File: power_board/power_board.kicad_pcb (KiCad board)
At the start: 2 copper layers, 165.3 x 121.3 mm, 66 parts, among them J1 PROG, J10 M4, J11 5V_1, J12 M5, J13 M6, J14 M7, J15 FAN, J16 Screw_Terminal_01x02, J17 MB_interface, J19 12V_1, J2 M1, J20 12V_2, J21 12V_3, J22 12V_4, J23 48V_1, J24 48V_2, J25 48V_3, J26 48V_4, J3 M2, J4 Conn_01x02_Female, J5 Conn_01x02_Female, J6 Conn_01x01_Male, J7 Conn_01x01_Male, J8 Screw_Terminal_01x02, J9 M3, Q1 2N3906, SW1 SW_Push, U1 ACS758xCB-050B-PFF, U2 ACS758xCB-050B-PFF, U3 MCP2515-EST, U4 MAX31855KASA, U5 MCP2551-I-SN, U6 BTS50085-1TMA, U7 ATmega328P-AU, U8 BTS50085-1TMA, U9 LM2596S-5, Y1 20Mhz, Y2 16Mhz

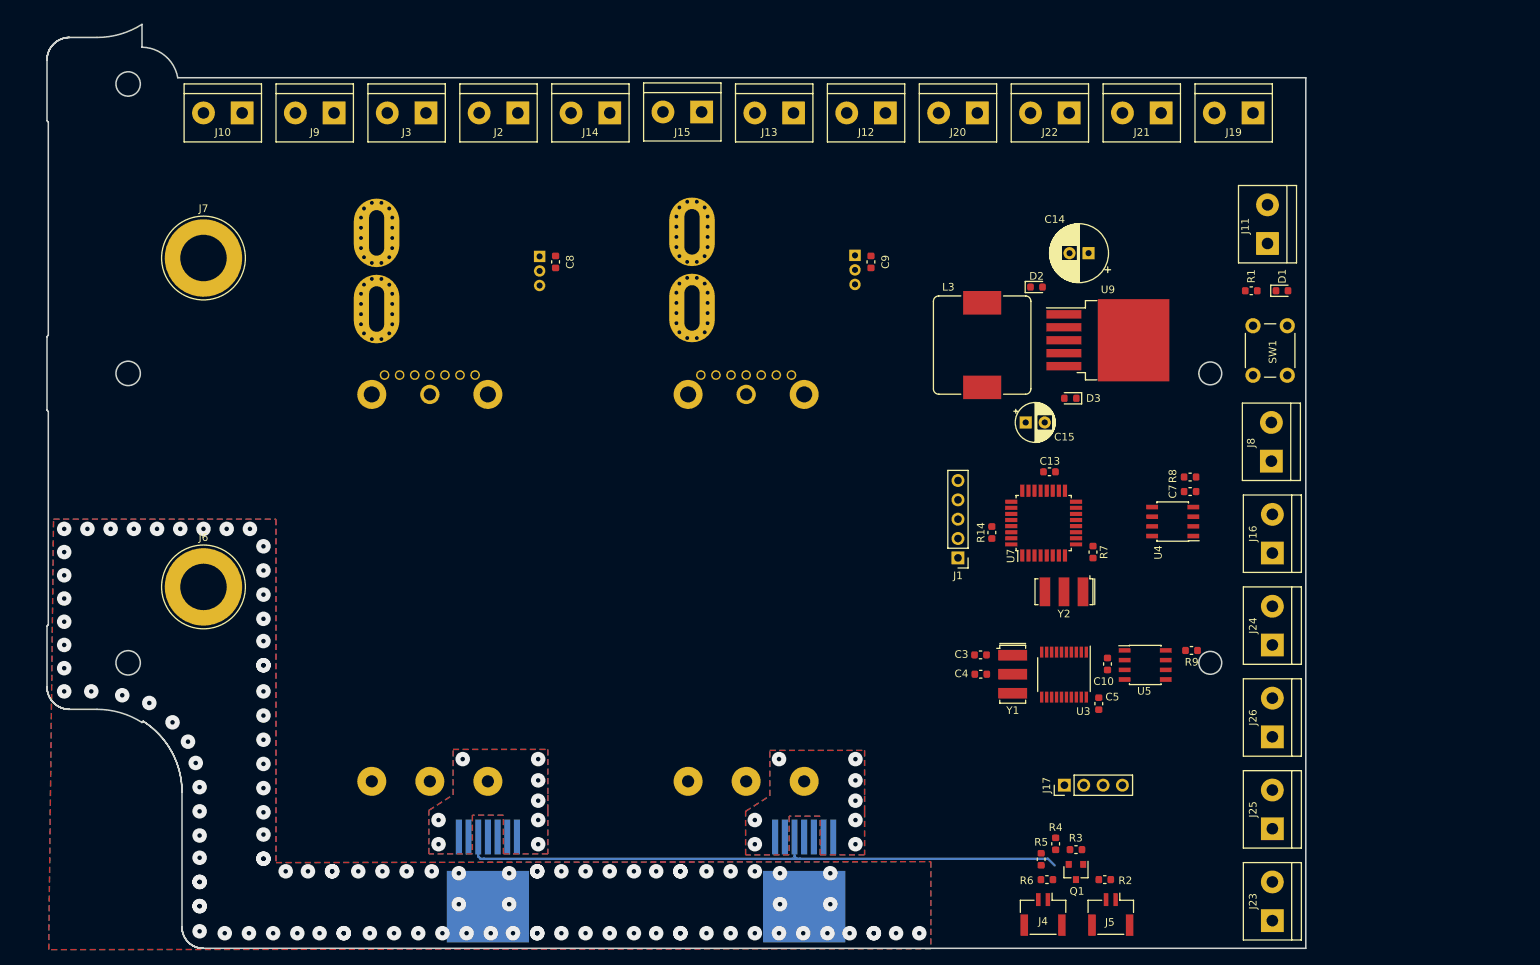
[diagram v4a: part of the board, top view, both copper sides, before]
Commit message: Finished high power routing
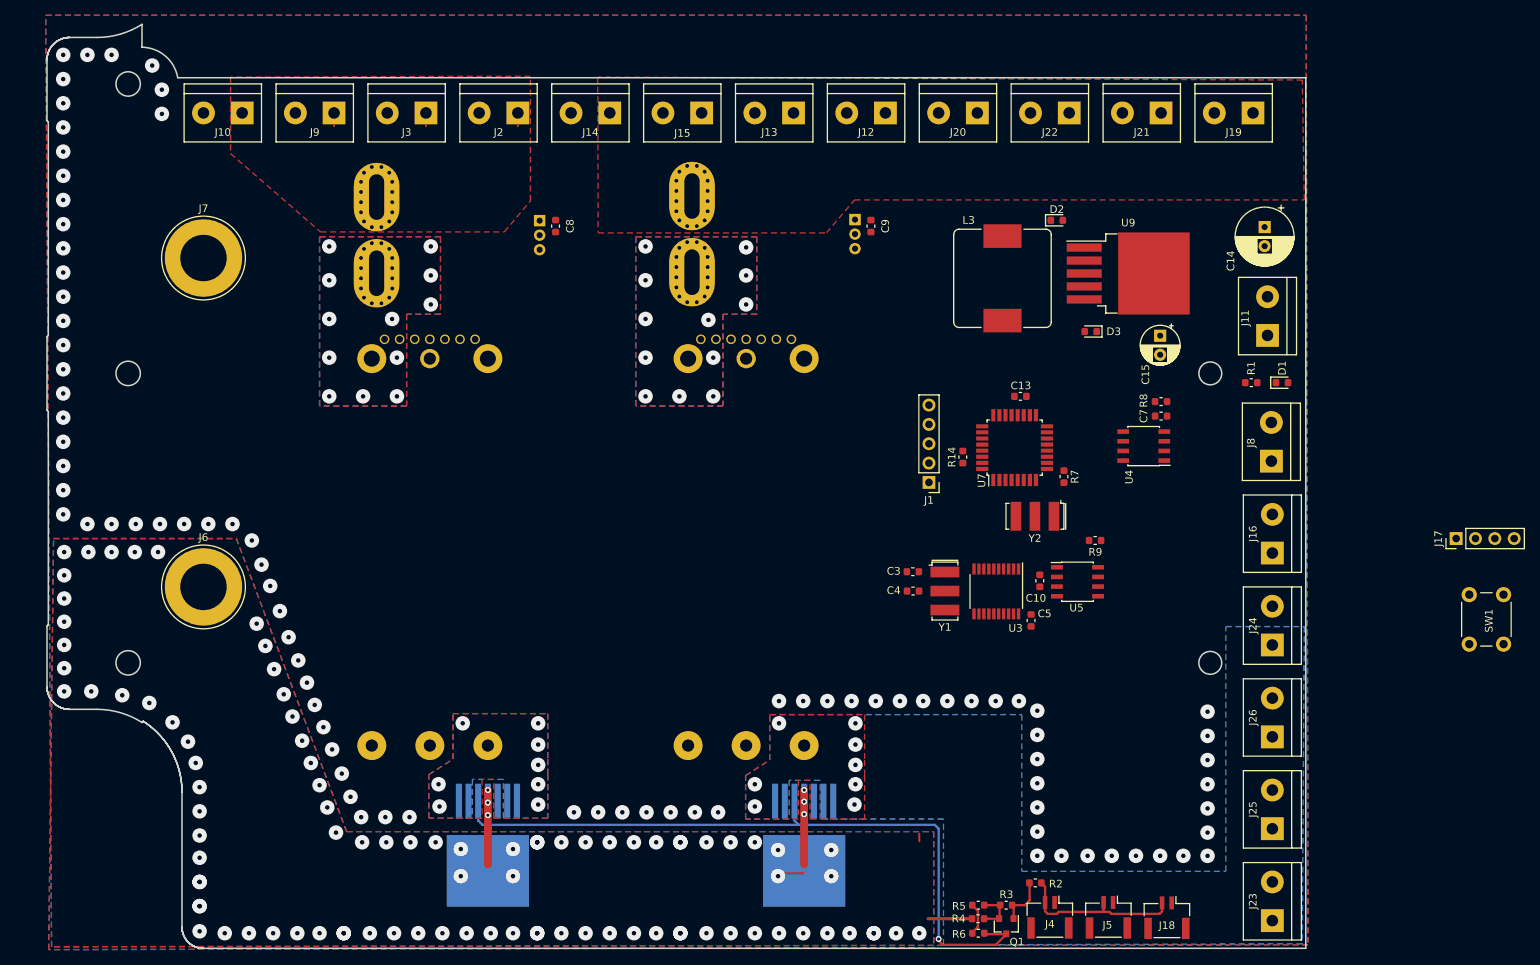
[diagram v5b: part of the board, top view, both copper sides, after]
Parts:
- added J18: Conn_01x02_Female, Connector_JST:JST_GH_BM02B-GHS-TBT_1x02-1MP_P1.25mm_Vertical, F.Cu at (207.8, 147.6)
- moved J17 60.8 mm to (245.7, 97.8)
- moved SW1 45.3 mm to (252.0, 105.2)
- moved C14 23.4 mm to (220.6, 56.9), turned to 270 degrees
- moved C15 21.0 mm to (206.9, 71.2), turned to 270 degrees
- moved R9 19.2 mm to (198.3, 98.0)
- moved R4 14.2 mm to (183.0, 147.7), turned to 180 degrees
- moved C10 14.1 mm to (191.1, 103.3)
- moved C5 14.1 mm to (189.9, 108.5)
- moved U3 14.1 mm to (185.4, 104.7)
- moved U5 14.1 mm to (196.0, 103.5)
- moved C3 14.1 mm to (174.4, 102.1)
- moved C4 14.1 mm to (174.4, 104.7)
- moved Y1 14.1 mm to (178.6, 104.7)
- moved J11 12.1 mm to (221.0, 71.1)
- moved D1 12.1 mm to (222.9, 77.3)
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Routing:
- net +48V: track 0.00 -> 29.6 mm, vias 109 -> 100
- net Net-(J18-Pad2): track 0.00 -> 22.2 mm
- net SHUTOFF: track 82.2 -> 94.4 mm, vias 0 -> 1
- net Net-(Q1-Pad1): track 0.00 -> 6.92 mm
- net +5VA: track 0.00 -> 6.10 mm
- net +12V: track 0.00 -> 5.25 mm
- net GNDREF: track 0.00 -> 4.34 mm, vias 0 -> 85
- net 12V_IN: vias 0 -> 12
- net 12VA_IN: vias 0 -> 12
- added copper zone on F.Cu, net +12V
- added copper zone on F.Cu, net +12VA
- added copper zone on B.Cu, net 12VA_IN
- added copper zone on F.Cu, net 12VA_IN
- added copper zone on B.Cu, net 12V_IN
- added copper zone on F.Cu, net 12V_IN
- added copper zone on B.Cu, net GNDREF
- added copper zone on F.Cu, net GNDREF

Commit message: Current sensor routing/finishing touches
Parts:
- moved J1 65.9 mm to (242.4, 89.5), turned to 270 degrees
- moved Y2 59.9 mm to (246.6, 74.2), turned to 270 degrees
- moved R14 58.0 mm to (238.9, 83.7), turned to 180 degrees
- moved R7 50.9 mm to (241.4, 70.4), turned to 0 degrees
- moved U7 50.6 mm to (237.6, 76.9), turned to 180 degrees
- moved C13 42.5 mm to (230.9, 76.1), turned to 270 degrees
- moved C5 21.2 mm to (211.1, 107.4)
- moved Y1 20.4 mm to (196.0, 94.0)
- moved U3 20.4 mm to (202.8, 94.1)
- moved C3 19.9 mm to (191.3, 91.6)
- moved C4 19.9 mm to (191.3, 94.1)
- moved C10 18.7 mm to (208.5, 96.7)
- moved U5 18.5 mm to (213.2, 96.6)
- moved R9 17.5 mm to (215.1, 93.0), turned to 0 degrees
- moved C7 8.52 mm to (215.4, 83.2)
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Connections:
- J16 pad 1: CANH -> CANL
- J16 pad 2: CANL -> CANH
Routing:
- net +5V: track 0.00 -> 88.6 mm, vias 0 -> 2
- net 12V_SENSE: track 0.00 -> 61.3 mm, vias 0 -> 2
- net 12VA_SENSE: track 0.00 -> 22.0 mm, vias 0 -> 1
- net GNDREF: vias 85 -> 97

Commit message: working on microcontroller routing
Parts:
- D2, D3: footprint Diode_SMD:D_0603_1608Metric -> Diode_SMD:D_SMB
- moved Y2 48.3 mm to (198.5, 78.2)
- moved C13 48.2 mm to (182.8, 79.0)
- moved U7 48.2 mm to (189.5, 79.8)
- moved R7 47.3 mm to (203.1, 98.0), turned to 270 degrees
- moved SW1 46.6 mm to (217.7, 73.7), turned to 0 degrees
- moved J17 41.4 mm to (204.9, 104.0)
- moved J1 40.9 mm to (206.4, 70.2), turned to 0 degrees
- moved C15 27.7 mm to (180.3, 63.2), turned to 90 degrees
- moved R14 26.5 mm to (215.7, 70.7)
- moved D3 15.4 mm to (182.4, 69.5), turned to 90 degrees
- moved D2 13.0 mm to (180.3, 56.3), turned to 180 degrees
- moved C5 11.3 mm to (204.9, 98.0)
- moved L3 5.53 mm to (191.4, 61.8)
- moved R1 4.83 mm to (223.9, 70.7), turned to 0 degrees
- moved D1 3.07 mm to (219.8, 70.7), turned to 180 degrees
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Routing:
- net +5V: track 88.6 -> 124.5 mm, vias 2 -> 3
- net Net-(C15-Pad1): track 0.00 -> 26.5 mm
- net Net-(D2-Pad1): track 0.00 -> 20.2 mm
- net GNDREF: track 4.34 -> 20.0 mm, vias 97 -> 101
- net Net-(J8-Pad2): track 0.00 -> 7.34 mm
- net CANH: track 0.00 -> 6.51 mm
- net CANL: track 0.00 -> 6.36 mm
- net Net-(J8-Pad1): track 0.00 -> 5.76 mm
- net TC_CS: track 0.00 -> 4.79 mm
- net CAN_CS: track 0.00 -> 2.37 mm
- net Net-(R9-Pad2): track 0.00 -> 1.75 mm

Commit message: finishing touches
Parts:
- Y2: footprint Crystal:Resonator_SMD-3Pin_7.2x3.0mm -> CSTCE16M0V53-R0:OSC_CSTCE16M0V53-R0
- moved C2 92.1 mm to (140.6, 139.6), turned to 90 degrees
- moved C1 30.7 mm to (69.2, 101.2), turned to 90 degrees
- moved R7 11.9 mm to (191.1, 97.8)
- moved Y1 11.9 mm to (183.0, 91.7)
- moved C3 11.9 mm to (178.2, 89.3)
- moved C4 11.9 mm to (178.3, 91.9)
- moved C5 11.9 mm to (192.9, 97.8)
- moved U3 11.9 mm to (189.7, 91.8)
- moved J17 8.14 mm to (196.7, 103.5)
- moved J1 3.39 mm to (203.1, 71.0)
- moved Y2 2.10 mm to (196.6, 77.3)
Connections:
- C1 pad 1: Net-(C1-Pad1) -> +48V
- C2 pad 1: 48V -> +48V
- J1 pad 3: TX -> RX
- J1 pad 4: RX -> TX
- J17 pad 1: +5V -> GNDREF
- J17 pad 4: GNDREF -> +5V
- REG1 pad 1: Net-(C1-Pad1) -> Net-(REG1-Pad1)
- U6 pad 1: Net-(C1-Pad1) -> Net-(REG1-Pad1)
- U6 pad 2: Net-(C1-Pad1) -> Net-(REG1-Pad1)
- U6 pad 6: Net-(C1-Pad1) -> Net-(REG1-Pad1)
- U6 pad 7: Net-(C1-Pad1) -> Net-(REG1-Pad1)
- U7 pad 1: RX_INT -> CAN_INT
- U7 pad 10: TC_CS -> Net-(U7-Pad10)
- U7 pad 2: Net-(U7-Pad2) -> TC_CS
- U7 pad 23: 12V_SENSE -> 12VA_SENSE
- U7 pad 24: 12VA_SENSE -> 12V_SENSE
- U7 pad 26: TX0RTS -> TX2RTS
- U7 pad 28: TX2RTS -> TX0RTS
- U7 pad 32: CAN_INT -> RX_INT
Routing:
- net GNDREF: track 20.0 -> 178.7 mm, vias 101 -> 119
- net +5V: track 124.5 -> 281.3 mm, vias 3 -> 5
- net RESET: track 0.00 -> 51.9 mm, vias 0 -> 3
- net SCK: track 0.00 -> 46.7 mm, vias 0 -> 4
- net MISO: track 0.00 -> 43.9 mm, vias 0 -> 2
- net CAN_RX: track 0.00 -> 34.3 mm, vias 0 -> 2
- net CAN_TX: track 0.00 -> 29.0 mm, vias 0 -> 3
- net CAN_CS: track 2.37 -> 27.4 mm, vias 0 -> 2
- net CAN_INT: track 0.00 -> 23.7 mm, vias 0 -> 2
- net RX_INT: track 0.00 -> 22.1 mm, vias 0 -> 2
- net CANH: track 6.51 -> 27.6 mm
- net MOSI: track 0.00 -> 20.9 mm, vias 0 -> 2
- net TC_CS: track 4.79 -> 25.4 mm
- net 12VA_SENSE: track 22.0 -> 42.4 mm
- net 12V_SENSE: track 61.3 -> 81.2 mm
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- added copper zone on B.Cu, net Net-(REG1-Pad1)
- added copper zone on F.Cu, net Net-(REG1-Pad1)
- removed copper zone on B.Cu, net Net-(C1-Pad1)
- removed copper zone on F.Cu, net Net-(C1-Pad1)
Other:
- rule trace_min: 0.2 -> 0.3048
